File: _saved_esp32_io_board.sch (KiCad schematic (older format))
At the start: 62 parts, among them J1 USB_B_Micro, J11 Conn_01x02, J12 Conn_01x02, J13 Conn_01x02, J14 Conn_01x02, J15 Conn_01x02, J16 Conn_01x02, J17 Conn_01x02, J18 Conn_01x02, J2 Conn_02x04_Counter_Clockwise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

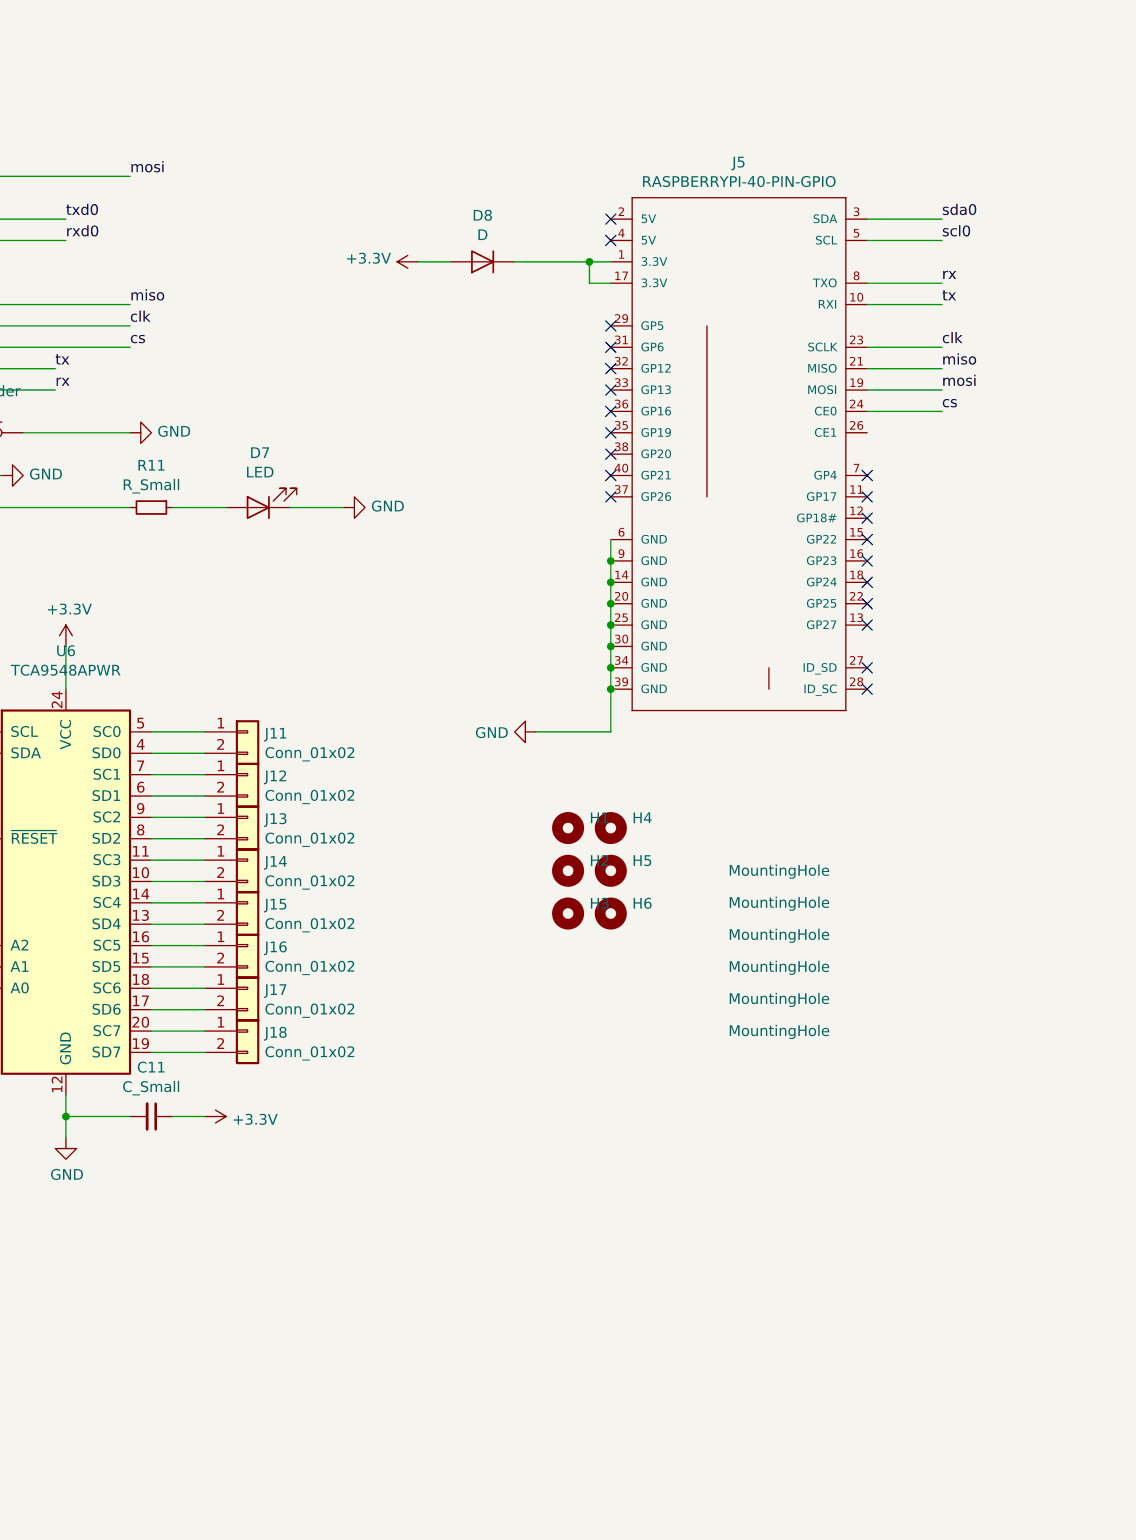
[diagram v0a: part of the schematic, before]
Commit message: raspberry pi integration
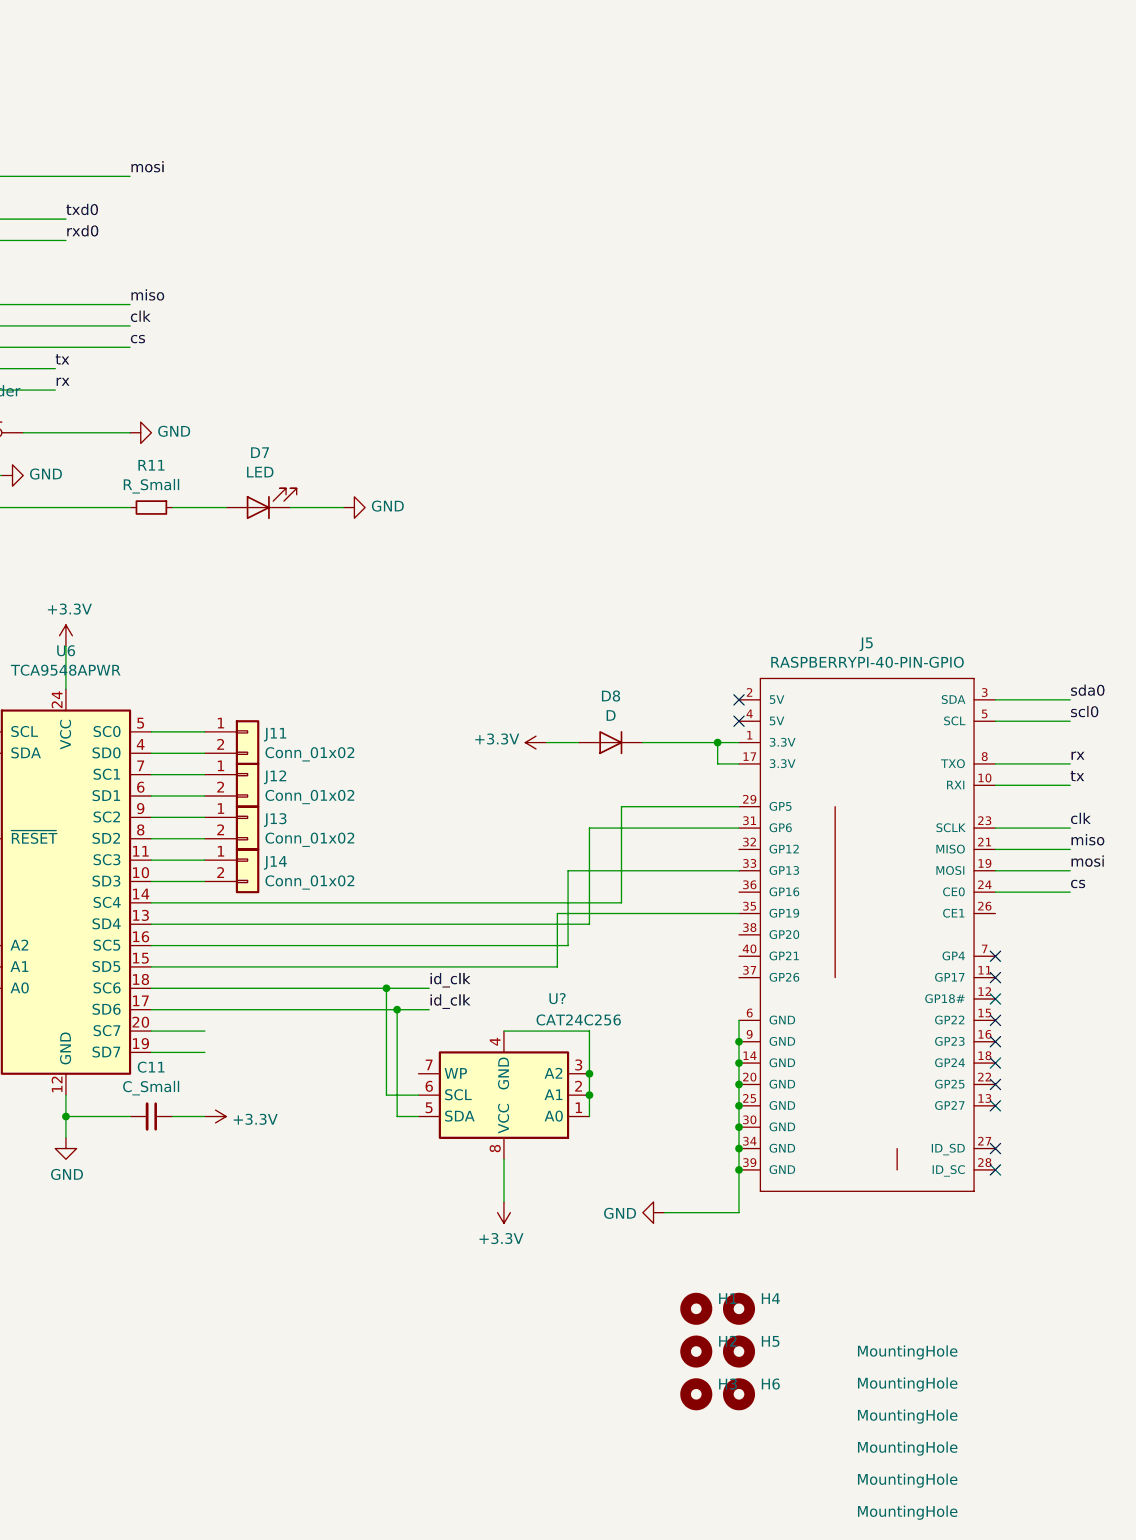
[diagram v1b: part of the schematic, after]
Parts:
- removed J15, J16, J17, J18: Conn_01x02, Connector_PinHeader_2.54mm:PinHeader_1x02_P2.54mm_Vertical, symbol Connector_Generic:Conn_01x02
- added U?: CAT24C256, symbol Memory_EEPROM:CAT24C256
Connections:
- net +3V3: now also U?.8 (VCC)
- net at J5.29 (GP5): now also U6.14 (SC4)
- net at J5.31 (GP6): now also U6.13 (SD4)
- net at J5.33 (GP13): now also U6.16 (SC5)
- net at J5.35 (GP19): now also U6.15 (SD5)
- net id_clk: now reaches U6.17 (SD6)
- net id_clk: now also U6.18 (SC6), U?.5 (SDA), U?.6 (SCL)
- new net: U?.1 (A0), U?.2 (A1), U?.3 (A2), U?.4 (GND)
- no-connect marks 39 -> 30
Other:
- moved on the sheet: D8, H1, H2, H3, H4, H5, H6, J5
